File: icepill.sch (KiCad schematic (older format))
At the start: 32 parts, among them IC1 iCE40UP5K-SG48, IC2 AZ1117H-1.2, J1 PMOD_1, J2 PMOD_2, J3 PMOD_3, J4 PMOD_4, J5 PMOD_5, J6 PMOD_6, J7 PMOD_7, J8 FPGA_A, J9 FPGA_B, U1 BlackPill, X1 M3_MOUNT, X2 M3_MOUNT, X3 M3_MOUNT, X4 M3_MOUNT

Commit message: Add power flags to PLL supply and LDO GND
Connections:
- no-connect marks 4 -> 5
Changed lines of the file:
@@
 	1200 2800 1200 2750
 Wire Wire Line
-	1200 2300 1200 2600
+	1200 2300 1200 2450
 $Comp
 L r:R R5
@@
 	-1   0    0    -1
 $EndComp
+NoConn ~ 3300 5750
+$Comp
+L pwr:PWR #FLG0101
+U 1 1 6040EACD
+P 3000 4300
+F 0 "#FLG0101" H 3000 4460 50  0001 C CNN
+F 1 "PWR" H 3000 4390 50  0001 C CNN
+F 2 "" H 3000 4300 50  0001 C CNN
+F 3 "" H 3000 4300 50  0001 C CNN
+	1    3000 4300
+	1    0    0    -1
+$EndComp
+Wire Wire Line
+	3000 4300 3000 4350
+$Comp
+L pwr:PWR #FLG0102
+U 1 1 604208C3
+P 1250 2450
+F 0 "#FLG0102" H 1250 2610 50  0001 C CNN
+F 1 "PWR" H 1250 2540 50  0001 C CNN
+F 2 "" H 1250 2450 50  0001 C CNN
+F 3 "" H 1250 2450 50  0001 C CNN
+	1    1250 2450
+	0    1    1    0
+$EndComp
+Wire Wire Line
+	1250 2450 1200 2450
+Connection ~ 1200 2450
+Wire Wire Line
+	1200 2450 1200 2600
 $EndSCHEMATC

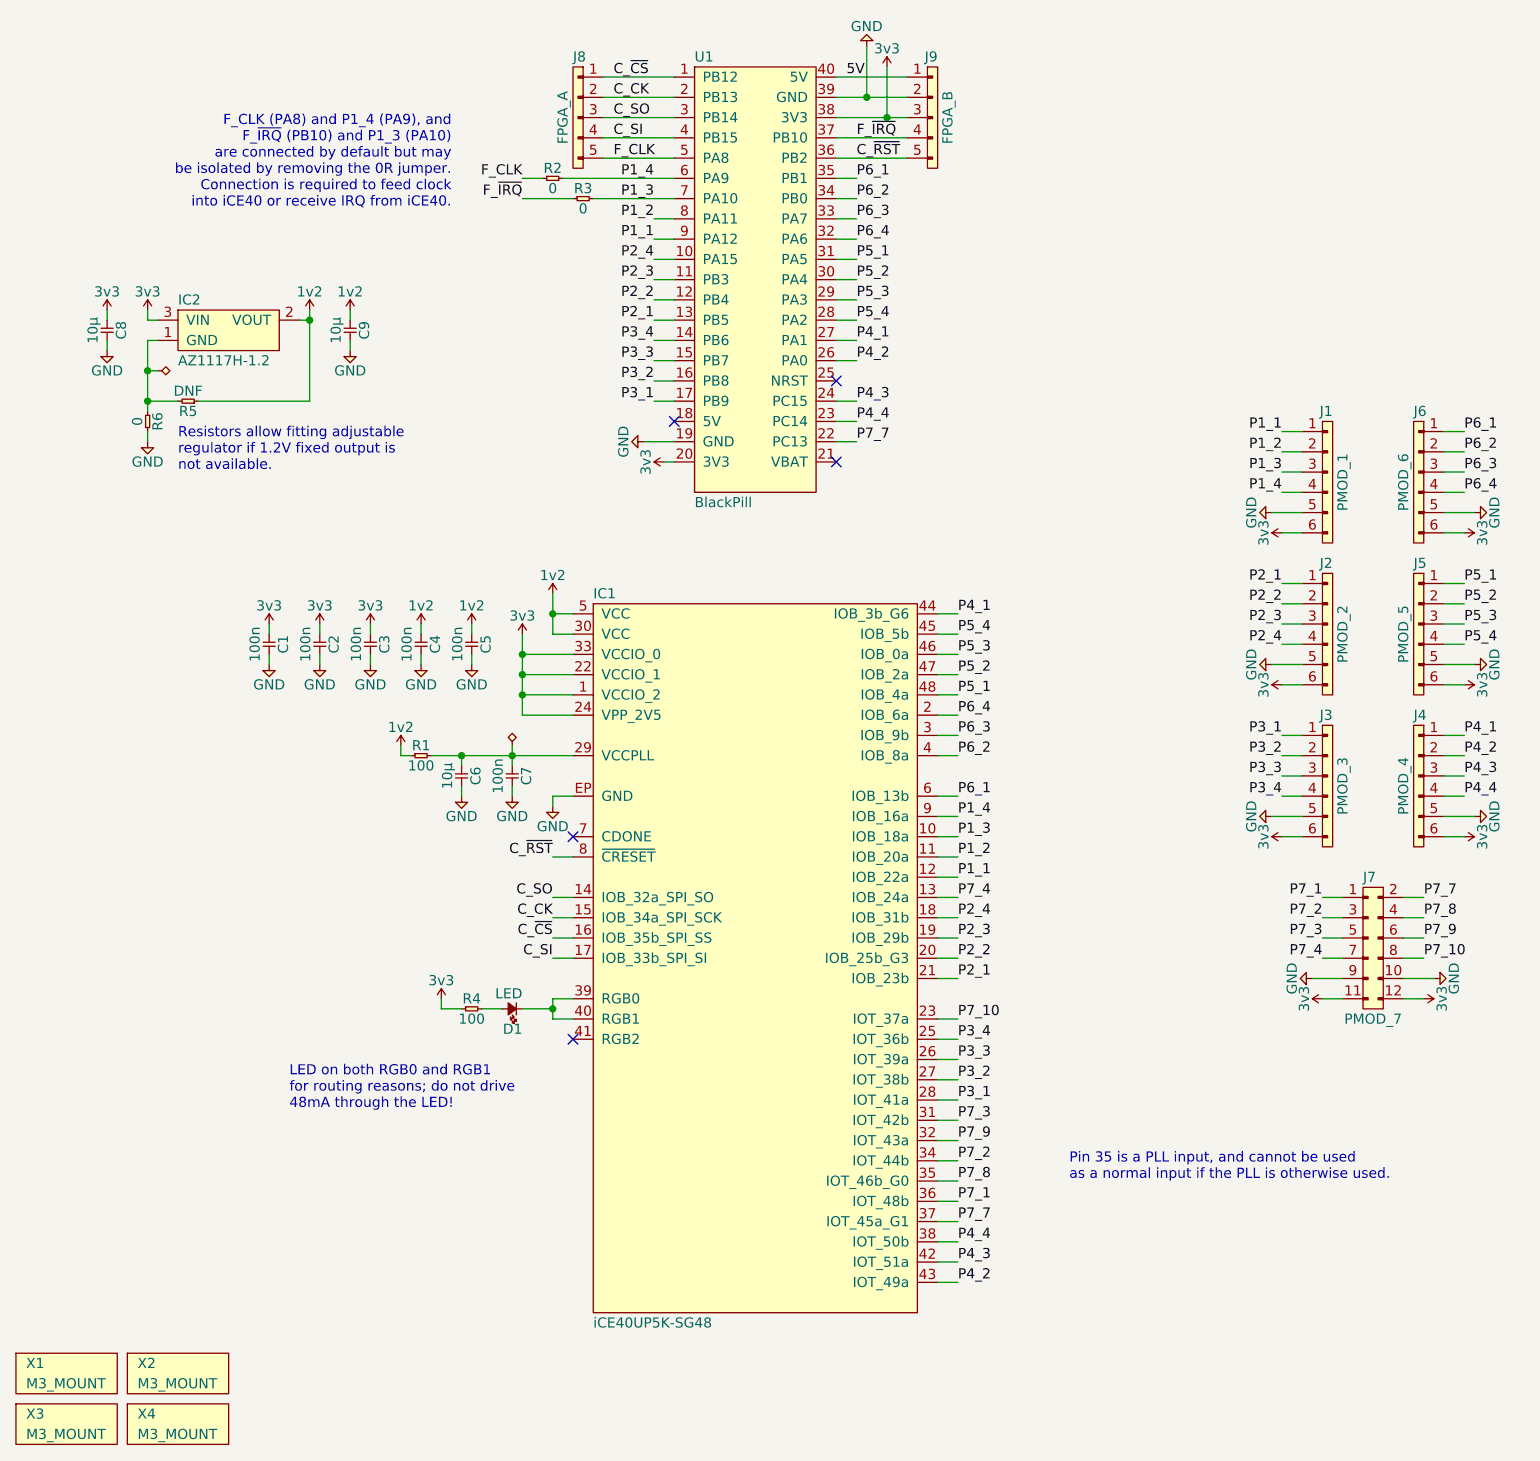
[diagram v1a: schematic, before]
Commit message: Address first revision feedback.
* MCO from STM32 now routes to GB3 (pin 20), a global input.
* Consequently F_CLK is now present at PMOD2.2.
* PC14 and PC15 no longer connected as they have an LSE on the Black Pill.
* F_IRQ moved to PMOD1.4.
* 0R resistors for selecting IRQ and CLK presence at PMODs changed to
  allow either STM32 or iCE40 to drive the PMOD pin, while the iCE40
  remains always connected to the other STM32 pin providing IRQ/CLK.
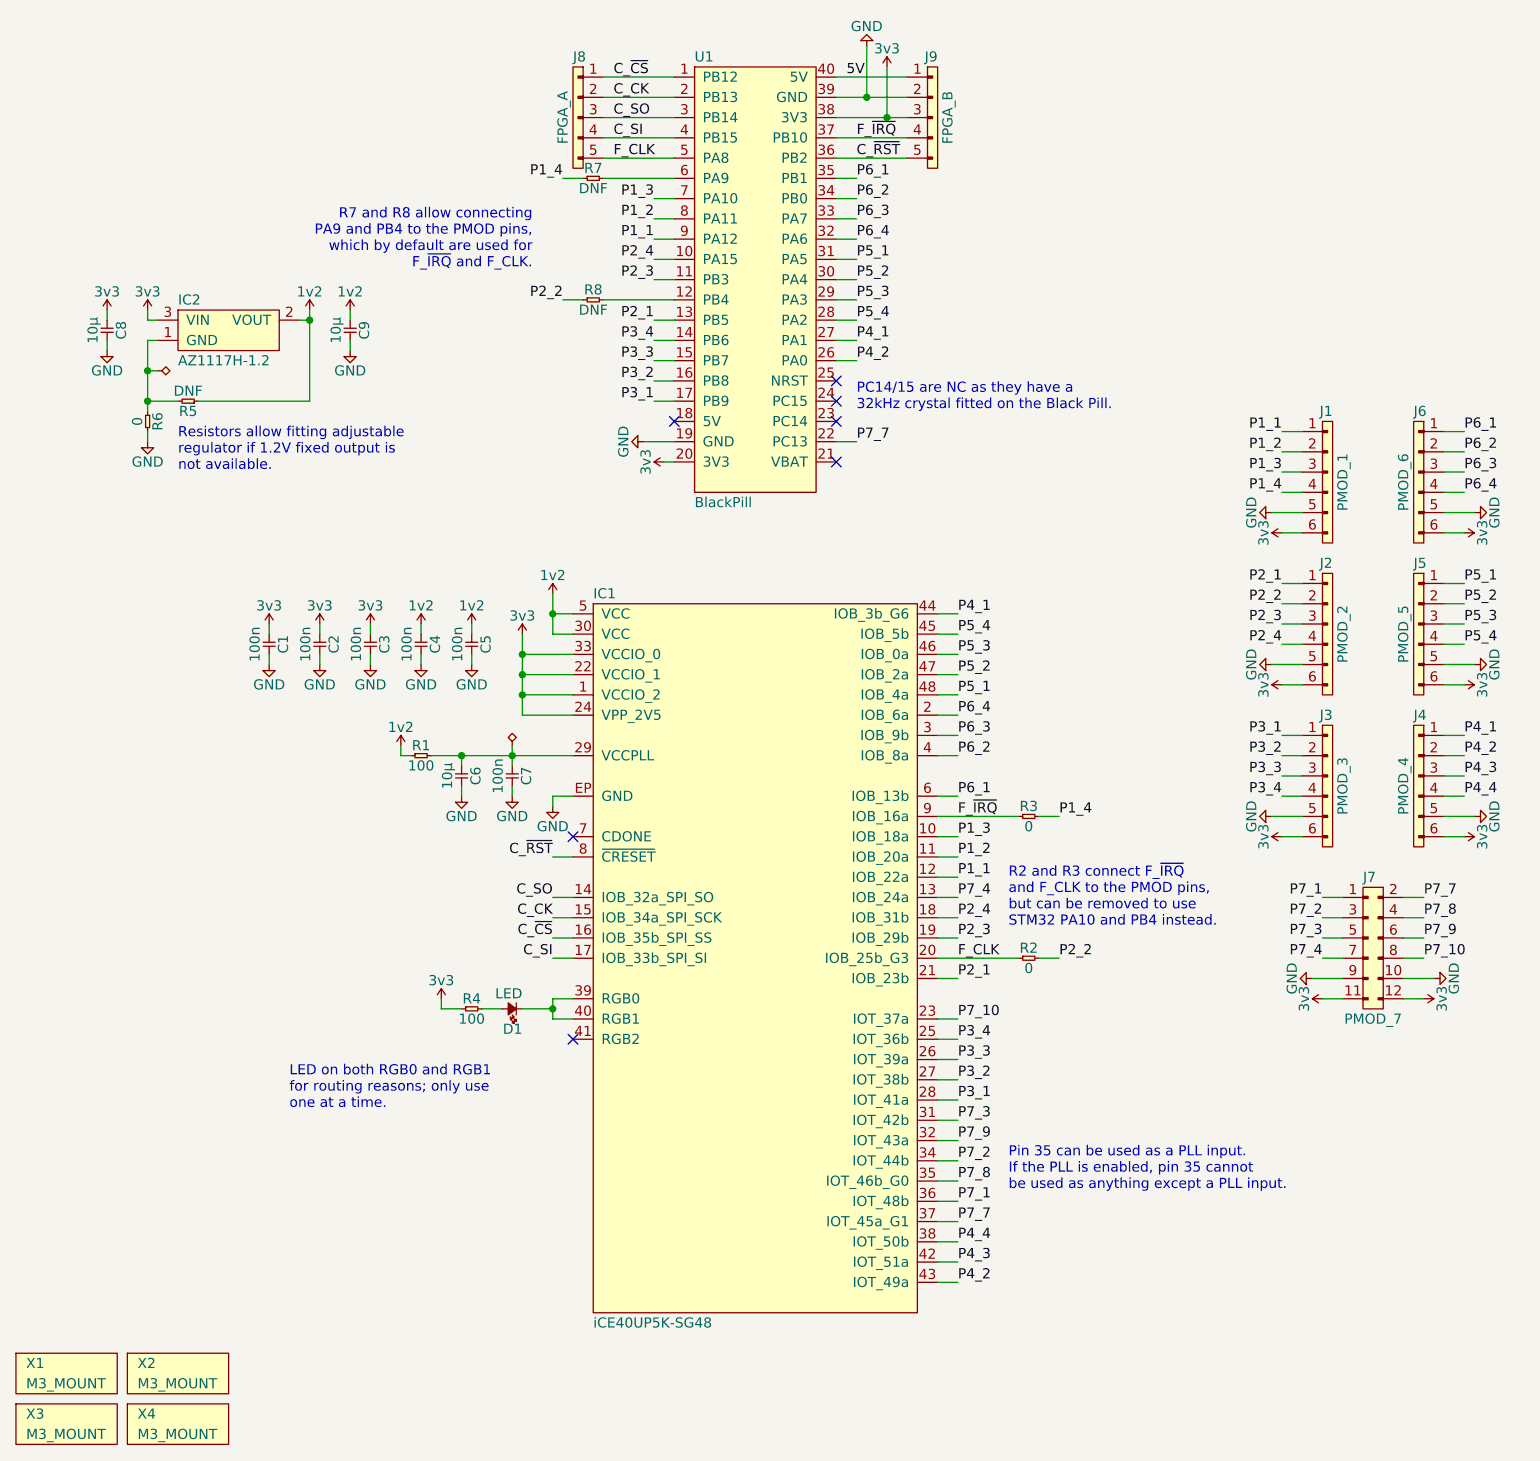
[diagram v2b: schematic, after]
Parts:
- added R7, R8: DNF, icepill:0603, symbol r:R
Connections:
- net F_CLK: now also IC1.20 (IOB_25b_G3)
- net F_~IRQ: now also IC1.9 (IOB_16a)
- net P1_3: no longer R3.2
- net P1_4: now also R3.2, R7.1; no longer IC1.9 (IOB_16a), R2.2, U1.6 (PA9)
- net P2_2: now also R2.2, R8.1; no longer IC1.20 (IOB_25b_G3), U1.12 (PB4)
- net P4_3: no longer U1.24 (PC15)
- net P4_4: no longer U1.23 (PC14)
- new net: R8.2, U1.12 (PB4)
- new net: R7.2, U1.6 (PA9)
- no-connect marks 5 -> 7
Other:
- note added: "LED on both RGB0 and RGB1\nfor routing reasons; only use\none at a time."
- note added: "PC14/15 are NC as they have a\n32kHz crystal fitted on the Black Pill."
- note added: "Pin 35 can be used as a PLL input.\nIf the PLL is enabled, pin 35 cannot\nbe used as anything except a PLL input."
- note added: "R2 and R3 connect F_~IRQ~\nand F_CLK to the PMOD pins,\nbut can be removed to use\nSTM32 PA10 and PB4 instead."
- note added: "R7 and R8 allow connecting\nPA9 and PB4 to the PMOD pins,\nwhich by default are used for\nF_~IRQ~ and F_CLK."
- note removed: "F_CLK (PA8) and P1_4 (PA9), and\nF_~IRQ~ (PB10) and P1_3 (PA10)\nare connected by default but may\nbe isolated by removing the 0R jumper.\nConnection is required to feed clock\ninto iCE40 or receive IRQ from iCE40."
- note removed: "LED on both RGB0 and RGB1\nfor routing reasons; do not drive\n48mA through the LED!"
- note removed: "Pin 35 is a PLL input, and cannot be used\nas a normal input if the PLL is otherwise used."
- moved on the sheet: R2, R3
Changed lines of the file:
@@
 	3200 4550 3300 4550
-Wire Wire Line
-	3300 4850 3200 4850
 Wire Wire Line
 	3300 5050 3200 5050
@@
 Text Label 3200 5350 2    50   ~ 0
 C_SI
-Text Notes 5750 6450 0    50   ~ 0
-Pin 35 is a PLL input, and cannot be used\nas a normal input if the PLL is otherwise used.
+Text Notes 5450 6500 0    50   ~ 0
+Pin 35 can be used as a PLL input.\nIf the PLL is enabled, pin 35 cannot\nbe used as anything except a PLL input.
 Text Label 3500 1200 0    50   ~ 0
 C_SO
@@
 	4600 2400 4700 2400
 Wire Wire Line
-	4700 2600 4600 2600
-Wire Wire Line
-	4600 2700 4700 2700
-Wire Wire Line
 	4700 2800 4600 2800
 Wire Wire Line
@@
 Wire Wire Line
 	3700 2000 3800 2000
-Wire Wire Line
-	3700 2100 3800 2100
 Wire Wire Line
 	3700 2200 3800 2200
@@
 Text Label 3700 1600 2    50   ~ 0
 P1_3
-Text Label 3700 1500 2    50   ~ 0
+Text Label 3250 1500 2    50   ~ 0
 P1_4
 Text Label 3700 2200 2    50   ~ 0
 P2_1
-Text Label 3700 2100 2    50   ~ 0
+Text Label 3250 2100 2    50   ~ 0
 P2_2
 Text Label 3700 2000 2    50   ~ 0
@@
 Text Label 4700 2400 0    50   ~ 0
 P4_2
-Text Label 4700 2600 0    50   ~ 0
-P4_3
-Text Label 4700 2700 0    50   ~ 0
-P4_4
 Text Label 4700 2800 0    50   ~ 0
 P7_7
-Text Label 5200 4650 0    50   ~ 0
+Text Label 5700 4650 0    50   ~ 0
 P1_4
 Text Label 5200 4750 0    50   ~ 0
@@
 Text Label 5200 5250 0    50   ~ 0
 P2_3
-Text Label 5200 5350 0    50   ~ 0
+Text Label 5700 5350 0    50   ~ 0
 P2_2
 Text Label 5200 5450 0    50   ~ 0
@@
 P1_1
 Wire Wire Line
-	5100 4650 5200 4650
-Wire Wire Line
-	5100 4750 5200 4750
-Wire Wire Line
 	5100 4850 5200 4850
 Wire Wire Line
@@
 Wire Wire Line
 	5100 5250 5200 5250
-Wire Wire Line
-	5100 5350 5200 5350
 Wire Wire Line
 	5100 5450 5200 5450
@@
 L r:R R3
 U 1 1 6028036E
-P 3300 1600
-F 0 "R3" H 3350 1650 50  0000 C CNN
-F 1 "0" H 3350 1550 50  0000 C CNN
-F 2 "icepill:0603" H 3300 1600 50  0001 C CNN
-F 3 "" H 3300 1600 50  0001 C CNN
-	1    3300 1600
-	1    0    0    -1
-$EndComp
-Wire Wire Line
-	3400 1600 3800 1600
-Text Label 3050 1600 2    50   ~ 0
+P 5500 4650
+F 0 "R3" H 5550 4700 50  0000 C CNN
+F 1 "0" H 5550 4600 50  0000 C CNN
+F 2 "icepill:0603" H 5500 4650 50  0001 C CNN
+F 3 "" H 5500 4650 50  0001 C CNN
+	1    5500 4650
+	1    0    0    -1
+$EndComp
+Text Label 5200 4650 0    50   ~ 0
 F_~IRQ
 Wire Wire Line
-	3050 1600 3300 1600
+	3250 1500 3350 1500
 Wire Wire Line
 	3450 1400 3800 1400
@@
 L r:R R2
 U 1 1 60296195
-P 3150 1500
-F 0 "R2" H 3200 1550 50  0000 C CNN
-F 1 "0" H 3200 1450 50  0000 C CNN
-F 2 "icepill:0603" H 3150 1500 50  0001 C CNN
-F 3 "" H 3150 1500 50  0001 C CNN
-	1    3150 1500
-	1    0    0    -1
-$EndComp
-Wire Wire Line
-	3250 1500 3800 1500
-Text Label 3050 1500 2    50   ~ 0
+P 5500 5350
+F 0 "R2" H 5550 5400 50  0000 C CNN
+F 1 "0" H 5550 5300 50  0000 C CNN
+F 2 "icepill:0603" H 5500 5350 50  0001 C CNN
+F 3 "" H 5500 5350 50  0001 C CNN
+	1    5500 5350
+	1    0    0    -1
+$EndComp
+Text Label 5200 5350 0    50   ~ 0
 F_CLK
-Wire Wire Line
-	3050 1500 3150 1500
-Text Notes 2700 1650 2    50   ~ 0
-F_CLK (PA8) and P1_4 (PA9), and\nF_~IRQ~ (PB10) and P1_3 (PA10)\nare connected by default but may\nbe isolated by removing the 0R jumper.\nConnection is required to feed clock\ninto iCE40 or receive IRQ from iCE40.
+Text Notes 3100 1950 2    50   ~ 0
+R7 and R8 allow connecting\nPA9 and PB4 to the PMOD pins,\nwhich by default are used for\nF_~IRQ~ and F_CLK.
 Wire Wire Line
 	3200 5550 3200 5600
@@
 	3200 5600 3200 5650
 Text Notes 1900 6100 0    50   ~ 0
-LED on both RGB0 and RGB1\nfor routing reasons; do not drive\n48mA through the LED!
+LED on both RGB0 and RGB1\nfor routing reasons; only use\none at a time.
 Wire Wire Line
 	3300 5550 3200 5550
@@
 Wire Wire Line
 	1200 2450 1200 2600
+Wire Wire Line
+	3200 4850 3300 4850
+NoConn ~ 4600 2600
+NoConn ~ 4600 2700
+Text Notes 4700 2650 0    50   ~ 0
+PC14/15 are NC as they have a\n32kHz crystal fitted on the Black Pill.
+$Comp
+L r:R R8
+U 1 1 5FB79896
+P 3350 2100
+F 0 "R8" H 3400 2150 50  0000 C CNN
+F 1 "DNF" H 3400 2050 50  0000 C CNN
+F 2 "icepill:0603" H 3350 2100 50  0001 C CNN
+F 3 "" H 3350 2100 50  0001 C CNN
+	1    3350 2100
+	1    0    0    -1
+$EndComp
+Wire Wire Line
+	3250 2100 3350 2100
+Wire Wire Line
+	3450 2100 3800 2100
+$Comp
+L r:R R7
+U 1 1 5FC0CF5E
+P 3350 1500
+F 0 "R7" H 3400 1550 50  0000 C CNN
+F 1 "DNF" H 3400 1450 50  0000 C CNN
+F 2 "icepill:0603" H 3350 1500 50  0001 C CNN
+F 3 "" H 3350 1500 50  0001 C CNN
+	1    3350 1500
+	1    0    0    -1
+$EndComp
+Wire Wire Line
+	5100 5350 5500 5350
+Wire Wire Line
+	5700 5350 5600 5350
+Text Notes 5450 5200 0    50   ~ 0
+R2 and R3 connect F_~IRQ~\nand F_CLK to the PMOD pins,\nbut can be removed to use\nSTM32 PA10 and PB4 instead.
+Wire Wire Line
+	5200 4750 5100 4750
+Wire Wire Line
+	5700 4650 5600 4650
+Wire Wire Line
+	5100 4650 5500 4650
+Wire Wire Line
+	3700 1600 3800 1600
+Wire Wire Line
+	3450 1500 3800 1500
 $EndSCHEMATC

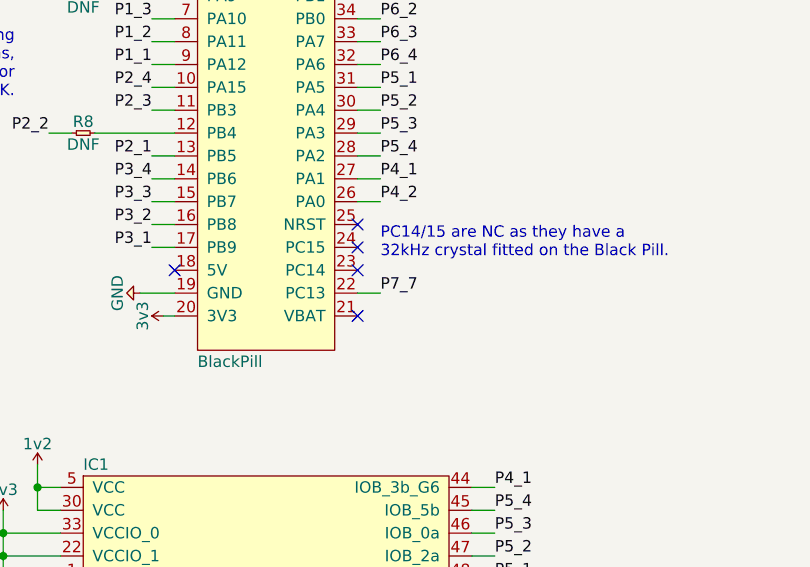
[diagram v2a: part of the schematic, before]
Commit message: Add pinout table to README, update render.
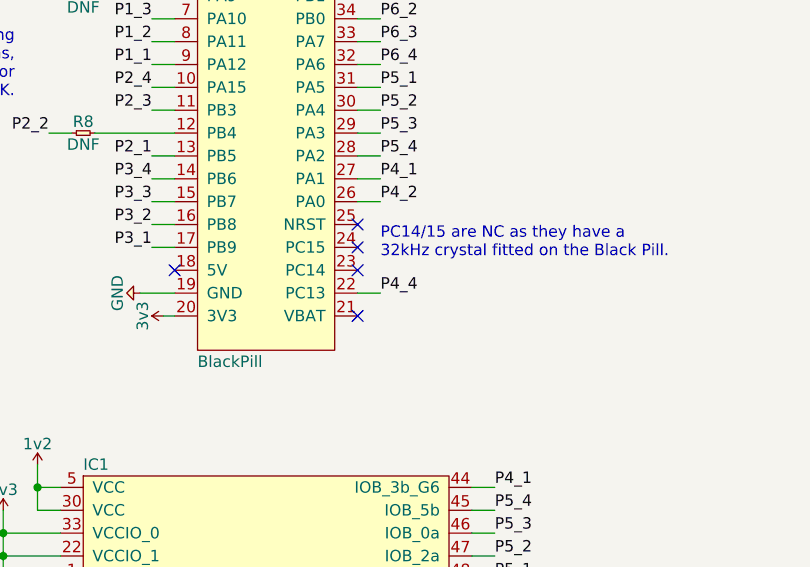
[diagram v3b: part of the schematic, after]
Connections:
- net P4_4: now also U1.22 (PC13)
- net P7_7: no longer U1.22 (PC13)
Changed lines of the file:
@@
 P4_2
 Text Label 4700 2800 0    50   ~ 0
-P7_7
+P4_4
 Text Label 5700 4650 0    50   ~ 0
 P1_4
